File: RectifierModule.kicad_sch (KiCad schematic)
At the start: 6 parts, among them J2 Transformer, J6 Rectifier Output

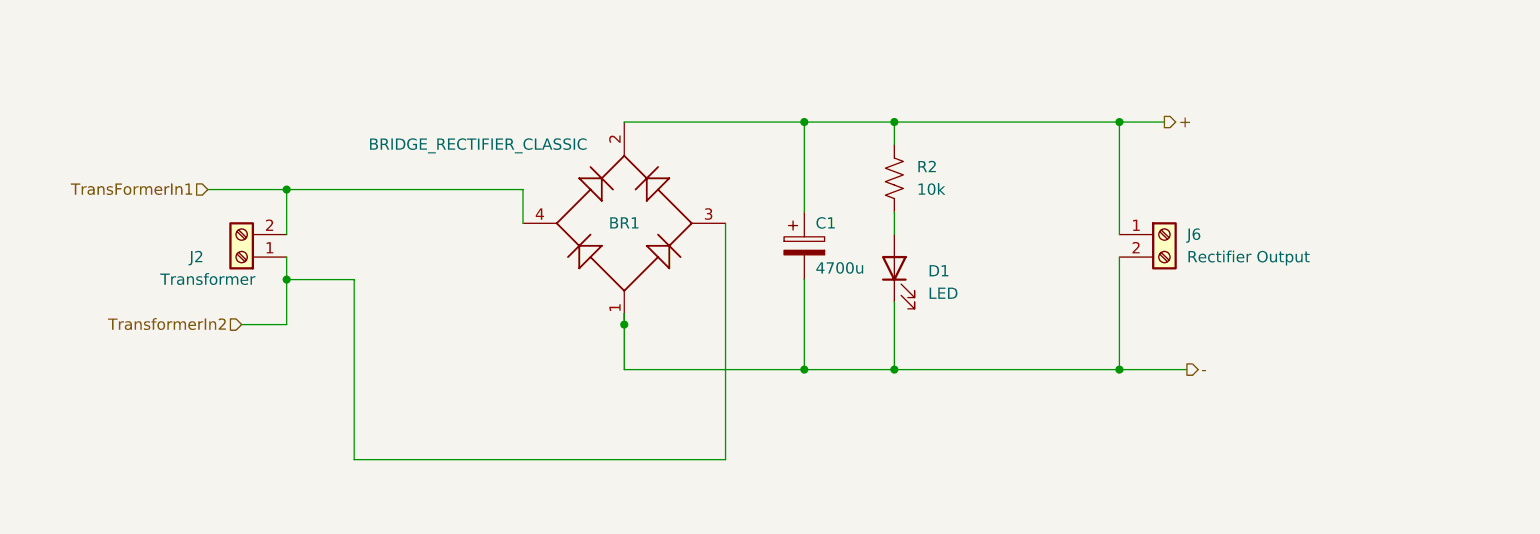
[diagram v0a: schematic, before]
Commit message: Updates to the schematic to make use of the centre tapped transformer to get negative rail.
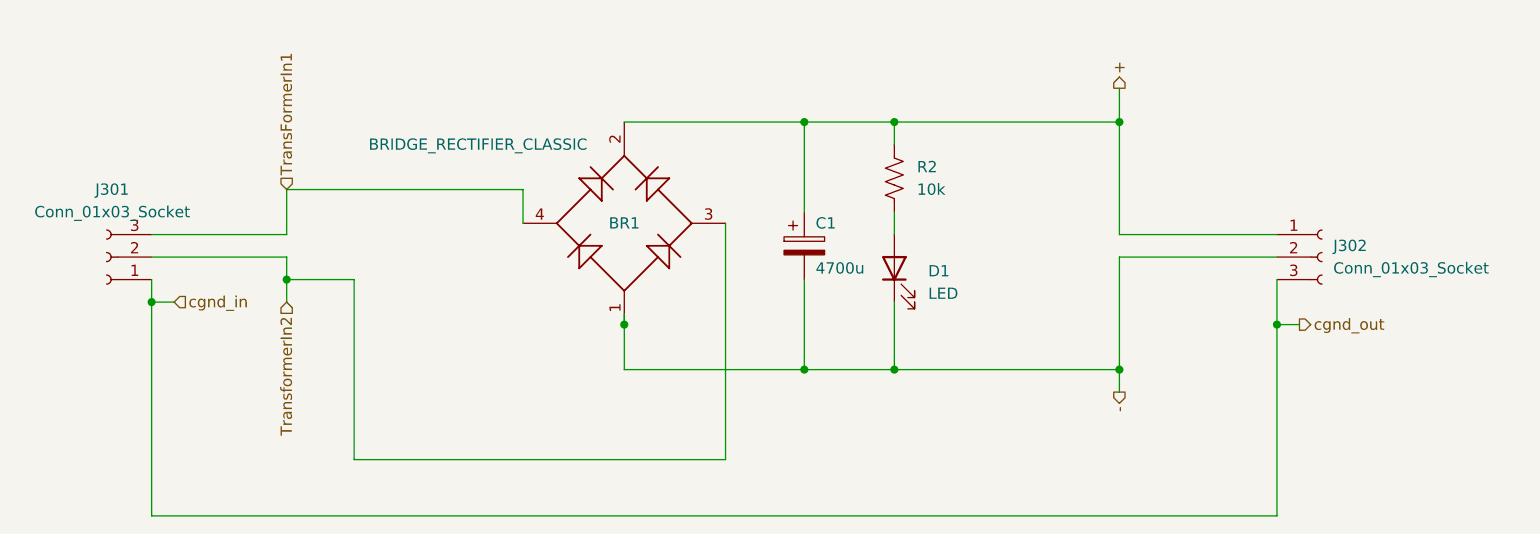
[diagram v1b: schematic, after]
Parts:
- removed J2: Transformer, TerminalBlock_Phoenix:TerminalBlock_Phoenix_MKDS-1,5-2-5.08_1x02_P5.08mm_Horizontal, symbol Connector:Screw_Terminal_01x02
- removed J6: Rectifier Output, TerminalBlock_Phoenix:TerminalBlock_Phoenix_MKDS-1,5-2-5.08_1x02_P5.08mm_Horizontal, symbol Connector:Screw_Terminal_01x02
- added J301, J302: Conn_01x03_Socket, symbol Connector:Conn_01x03_Socket
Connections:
- net +: now also J302.1 (Pin_1)
- net -: now also J302.2 (Pin_2)
- net TransFormerIn1: now also J301.3 (Pin_3)
- net TransformerIn2: now also J301.2 (Pin_2)
- new net cgnd_in: J301.1 (Pin_1), J302.3 (Pin_3)
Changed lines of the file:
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@@
   (junction (at 78.74 63.5) (diameter 0) (color 0 0 0 0)
   )
+  (junction (at 152.4 63.5) (diameter 0) (color 0 0 0 0)
+  )
   (junction (at 134.62 40.64) (diameter 0) (color 0 0 0 0)
   )
   (junction (at 109.22 68.58) (diameter 0) (color 0 0 0 0)
   )
+  (junction (at 40.64 58.42) (diameter 0) (color 0 0 0 0)
+  )
   (junction (at 109.22 40.64) (diameter 0) (color 0 0 0 0)
   )
   (junction (at 99.06 40.64) (diameter 0) (color 0 0 0 0)
   )
-  (junction (at 40.64 48.26) (diameter 0) (color 0 0 0 0)
+  (junction (at 25.4 60.96) (diameter 0) (color 0 0 0 0)
   )
   (junction (at 134.62 68.58) (diameter 0) (color 0 0 0 0)
   )
-  (junction (at 40.64 58.42) (diameter 0) (color 0 0 0 0)
-  )
-  (wire (pts (xy 35.56 63.5) (xy 40.64 63.5))
-    (stroke (width 0) (type default))
-  )
-  (wire (pts (xy 31.75 48.26) (xy 40.64 48.26))
+  (wire (pts (xy 25.4 58.42) (xy 25.4 60.96))
+    (stroke (width 0) (type default))
+  )
+  (wire (pts (xy 134.62 71.12) (xy 134.62 68.58))
+    (stroke (width 0) (type default))
+  )
+  (wire (pts (xy 134.62 55.88) (xy 152.4 55.88))
     (stroke (width 0) (type default))
   )
@@
     (stroke (width 0) (type default))
   )
+  (wire (pts (xy 25.4 85.09) (xy 152.4 85.09))
+    (stroke (width 0) (type default))
+  )
   (wire (pts (xy 90.17 78.74) (xy 48.26 78.74))
     (stroke (width 0) (type default))
   )
+  (wire (pts (xy 27.94 60.96) (xy 25.4 60.96))
+    (stroke (width 0) (type default))
+  )
+  (wire (pts (xy 25.4 55.88) (xy 40.64 55.88))
+    (stroke (width 0) (type default))
+  )
+  (wire (pts (xy 152.4 85.09) (xy 152.4 63.5))
+    (stroke (width 0) (type default))
+  )
   (wire (pts (xy 67.31 48.26) (xy 67.31 52.07))
     (stroke (width 0) (type default))
@@
     (stroke (width 0) (type default))
   )
+  (wire (pts (xy 152.4 63.5) (xy 152.4 58.42))
+    (stroke (width 0) (type default))
+  )
   (wire (pts (xy 78.74 40.64) (xy 99.06 40.64))
     (stroke (width 0) (type default))
@@
     (stroke (width 0) (type default))
   )
-  (wire (pts (xy 139.7 40.64) (xy 134.62 40.64))
-    (stroke (width 0) (type default))
-  )
   (wire (pts (xy 134.62 40.64) (xy 134.62 53.34))
     (stroke (width 0) (type default))
@@
     (stroke (width 0) (type default))
   )
+  (wire (pts (xy 25.4 53.34) (xy 40.64 53.34))
+    (stroke (width 0) (type default))
+  )
   (wire (pts (xy 99.06 40.64) (xy 99.06 50.8))
     (stroke (width 0) (type default))
@@
     (stroke (width 0) (type default))
   )
+  (wire (pts (xy 25.4 60.96) (xy 25.4 85.09))
+    (stroke (width 0) (type default))
+  )
+  (wire (pts (xy 40.64 55.88) (xy 40.64 58.42))
+    (stroke (width 0) (type default))
+  )
   (wire (pts (xy 99.06 68.58) (xy 109.22 68.58))
     (stroke (width 0) (type default))
   )
-  (wire (pts (xy 40.64 63.5) (xy 40.64 58.42))
+  (wire (pts (xy 134.62 53.34) (xy 152.4 53.34))
+    (stroke (width 0) (type default))
+  )
+  (wire (pts (xy 40.64 60.96) (xy 40.64 58.42))
     (stroke (width 0) (type default))
   )
@@
     (stroke (width 0) (type default))
   )
+  (wire (pts (xy 134.62 36.83) (xy 134.62 40.64))
+    (stroke (width 0) (type default))
+  )
   (wire (pts (xy 48.26 78.74) (xy 48.26 58.42))
     (stroke (width 0) (type default))
   )
-  (wire (pts (xy 40.64 58.42) (xy 40.64 55.88))
+  (wire (pts (xy 152.4 63.5) (xy 154.94 63.5))
     (stroke (width 0) (type default))
   )
@@
     (stroke (width 0) (type default))
   )
-  (wire (pts (xy 142.24 68.58) (xy 134.62 68.58))
-    (stroke (width 0) (type default))
-  )
-  (hierarchical_label "TransFormerIn1" (shape input) (at 31.75 48.26 180) (fields_autoplaced)
+  (hierarchical_label "TransFormerIn1" (shape input) (at 40.64 48.26 90) (fields_autoplaced)
+    (effects (font (size 1.27 1.27)) (justify left))
+  )
+  (hierarchical_label "TransformerIn2" (shape input) (at 40.64 60.96 270) (fields_autoplaced)
     (effects (font (size 1.27 1.27)) (justify right))
   )
-  (hierarchical_label "TransformerIn2" (shape input) (at 35.56 63.5 180) (fields_autoplaced)
+  (hierarchical_label "-" (shape output) (at 134.62 71.12 270) (fields_autoplaced)
     (effects (font (size 1.27 1.27)) (justify right))
   )
-  (hierarchical_label "-" (shape output) (at 142.24 68.58 0) (fields_autoplaced)
+  (hierarchical_label "cgnd_out" (shape output) (at 154.94 63.5 0) (fields_autoplaced)
     (effects (font (size 1.27 1.27)) (justify left))
   )
-  (hierarchical_label "+" (shape output) (at 139.7 40.64 0) (fields_autoplaced)
+  (hierarchical_label "+" (shape output) (at 134.62 36.83 90) (fields_autoplaced)
+    (effects (font (size 1.27 1.27)) (justify left))
+  )
+  (hierarchical_label "cgnd_in" (shape input) (at 27.94 60.96 0) (fields_autoplaced)
     (effects (font (size 1.27 1.27)) (justify left))
   )
@@
         )
         (path "/85225bbb-a12f-4483-ac90-767368bd8ae2/eccd6a13-cab4-4dd0-a5ba-dea4375f28d6"
-          (reference "BR1") (unit 1)
-        )
-      )
-    )
-  )
-  (symbol (lib_id "Connector:Screw_Terminal_01x02") (at 139.7 53.34 0) (unit 1)
+          (reference "BR301") (unit 1)
+        )
+      )
+    )
+  )
+  (symbol (lib_id "Connector:Conn_01x03_Socket") (at 157.48 55.88 0) (unit 1)
     (in_bom yes) (on_board yes) (dnp no) (fields_autoplaced)
-    (property "Reference" "J6" (at 142.24 53.34 0)
-      (effects (font (size 1.27 1.27)) (justify left))
-    )
-    (property "Value" "Rectifier  Output" (at 142.24 55.88 0)
-      (effects (font (size 1.27 1.27)) (justify left))
-    )
-    (property "Footprint" "TerminalBlock_Phoenix:TerminalBlock_Phoenix_MKDS-1,5-2-5.08_1x02_P5.08mm_Horizontal" (at 139.7 53.34 0)
-      (effects (font (size 1.27 1.27)) hide)
-    )
-    (property "Datasheet" "~" (at 139.7 53.34 0)
-      (effects (font (size 1.27 1.27)) hide)
-    )
-    (pin "1")
-    (pin "2")
-    (instances
-      (project "VariablePowerSupply"
-        (path "/769c317f-c67c-457d-a7ba-32e6f8df4c49"
-          (reference "J6") (unit 1)
-        )
-      )
-      (project "BenchPowerSupply"
-        (path "/85225bbb-a12f-4483-ac90-767368bd8ae2"
-          (reference "J4") (unit 1)
-        )
-        (path "/85225bbb-a12f-4483-ac90-767368bd8ae2/eccd6a13-cab4-4dd0-a5ba-dea4375f28d6"
-          (reference "J4") (unit 1)
+    (property "Reference" "J302" (at 158.75 54.61 0)
+      (effects (font (size 1.27 1.27)) (justify left))
+    )
+    (property "Value" "Conn_01x03_Socket" (at 158.75 57.15 0)
+      (effects (font (size 1.27 1.27)) (justify left))
+    )
+    (property "Footprint" "" (at 157.48 55.88 0)
+      (effects (font (size 1.27 1.27)) hide)
+    )
+    (property "Datasheet" "~" (at 157.48 55.88 0)
+      (effects (font (size 1.27 1.27)) hide)
+    )
+    (pin "1")
+    (pin "2")
+    (pin "3")
+    (instances
+      (project "BenchPowerSupply"
+        (path "/85225bbb-a12f-4483-ac90-767368bd8ae2/eccd6a13-cab4-4dd0-a5ba-dea4375f28d6"
+          (reference "J302") (unit 1)
         )
       )
@@
         )
         (path "/85225bbb-a12f-4483-ac90-767368bd8ae2/eccd6a13-cab4-4dd0-a5ba-dea4375f28d6"
-          (reference "R1") (unit 1)
+          (reference "R301") (unit 1)
         )
       )
@@
         )
         (path "/85225bbb-a12f-4483-ac90-767368bd8ae2/eccd6a13-cab4-4dd0-a5ba-dea4375f28d6"
-          (reference "C1") (unit 1)
-        )
-      )
-    )
-  )
-  (symbol (lib_id "Connector:Screw_Terminal_01x02") (at 35.56 55.88 180) (unit 1)
-    (in_bom yes) (on_board yes) (dnp no)
-    (property "Reference" "J2" (at 30.48 55.88 0)
+          (reference "C301") (unit 1)
+        )
+      )
+    )
+  )
+  (symbol (lib_id "Connector:Conn_01x03_Socket") (at 20.32 55.88 180) (unit 1)
+    (in_bom yes) (on_board yes) (dnp no) (fields_autoplaced)
+    (property "Reference" "J301" (at 20.955 48.26 0)
       (effects (font (size 1.27 1.27)))
     )
-    (property "Value" "Transformer" (at 31.75 58.42 0)
+    (property "Value" "Conn_01x03_Socket" (at 20.955 50.8 0)
       (effects (font (size 1.27 1.27)))
     )
-    (property "Footprint" "TerminalBlock_Phoenix:TerminalBlock_Phoenix_MKDS-1,5-2-5.08_1x02_P5.08mm_Horizontal" (at 35.56 55.88 0)
-      (effects (font (size 1.27 1.27)) hide)
-    )
-    (property "Datasheet" "~" (at 35.56 55.88 0)
-      (effects (font (size 1.27 1.27)) hide)
-    )
-    (pin "1")
-    (pin "2")
-    (instances
-      (project "VariablePowerSupply"
-        (path "/769c317f-c67c-457d-a7ba-32e6f8df4c49"
-          (reference "J2") (unit 1)
-        )
-      )
-      (project "BenchPowerSupply"
-        (path "/85225bbb-a12f-4483-ac90-767368bd8ae2"
-          (reference "J1") (unit 1)
-        )
-        (path "/85225bbb-a12f-4483-ac90-767368bd8ae2/eccd6a13-cab4-4dd0-a5ba-dea4375f28d6"
-          (reference "J1") (unit 1)
+    (property "Footprint" "" (at 20.32 55.88 0)
+      (effects (font (size 1.27 1.27)) hide)
+    )
+    (property "Datasheet" "~" (at 20.32 55.88 0)
+      (effects (font (size 1.27 1.27)) hide)
+    )
+    (pin "1")
+    (pin "2")
+    (pin "3")
+    (instances
+      (project "BenchPowerSupply"
+        (path "/85225bbb-a12f-4483-ac90-767368bd8ae2/eccd6a13-cab4-4dd0-a5ba-dea4375f28d6"
+          (reference "J301") (unit 1)
         )
       )
@@
         )
         (path "/85225bbb-a12f-4483-ac90-767368bd8ae2/eccd6a13-cab4-4dd0-a5ba-dea4375f28d6"
-          (reference "D1") (unit 1)
-        )
-      )
+          (reference "D301") (unit 1)
+        )
+      )
